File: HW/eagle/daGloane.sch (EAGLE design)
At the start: 44 parts, among them IC1 STM32F103CBT6, IC3 FT232RL, IC5 UA78M05DCY

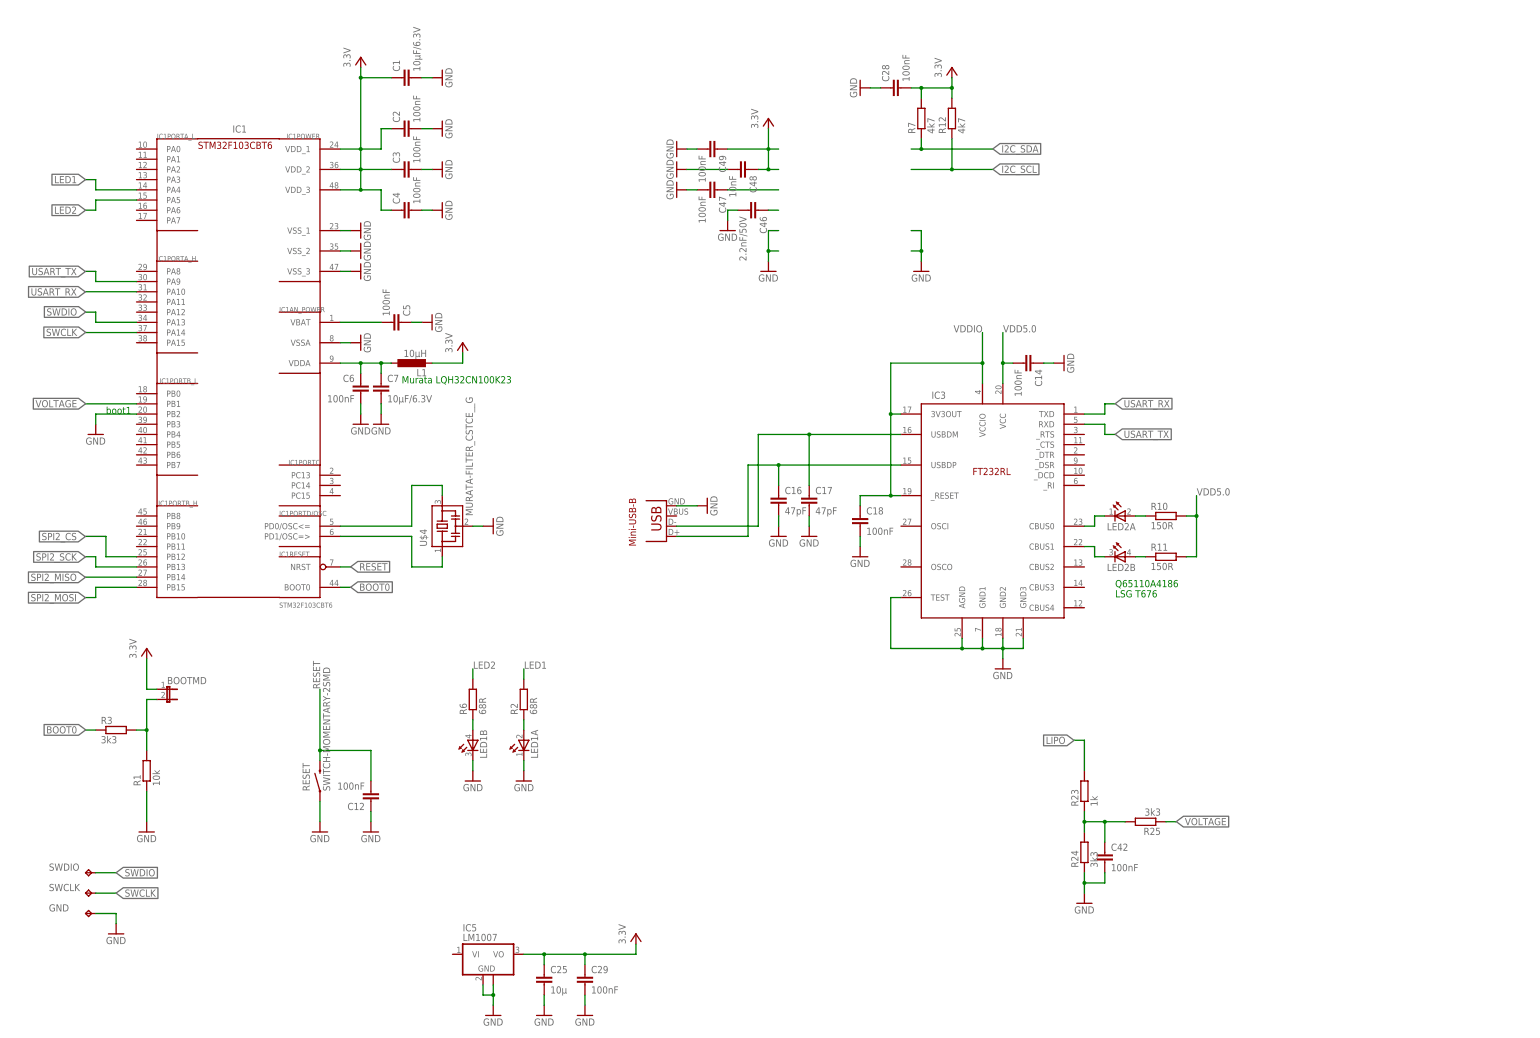
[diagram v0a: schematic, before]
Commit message: USB2UART interface replaced MPU6000 added
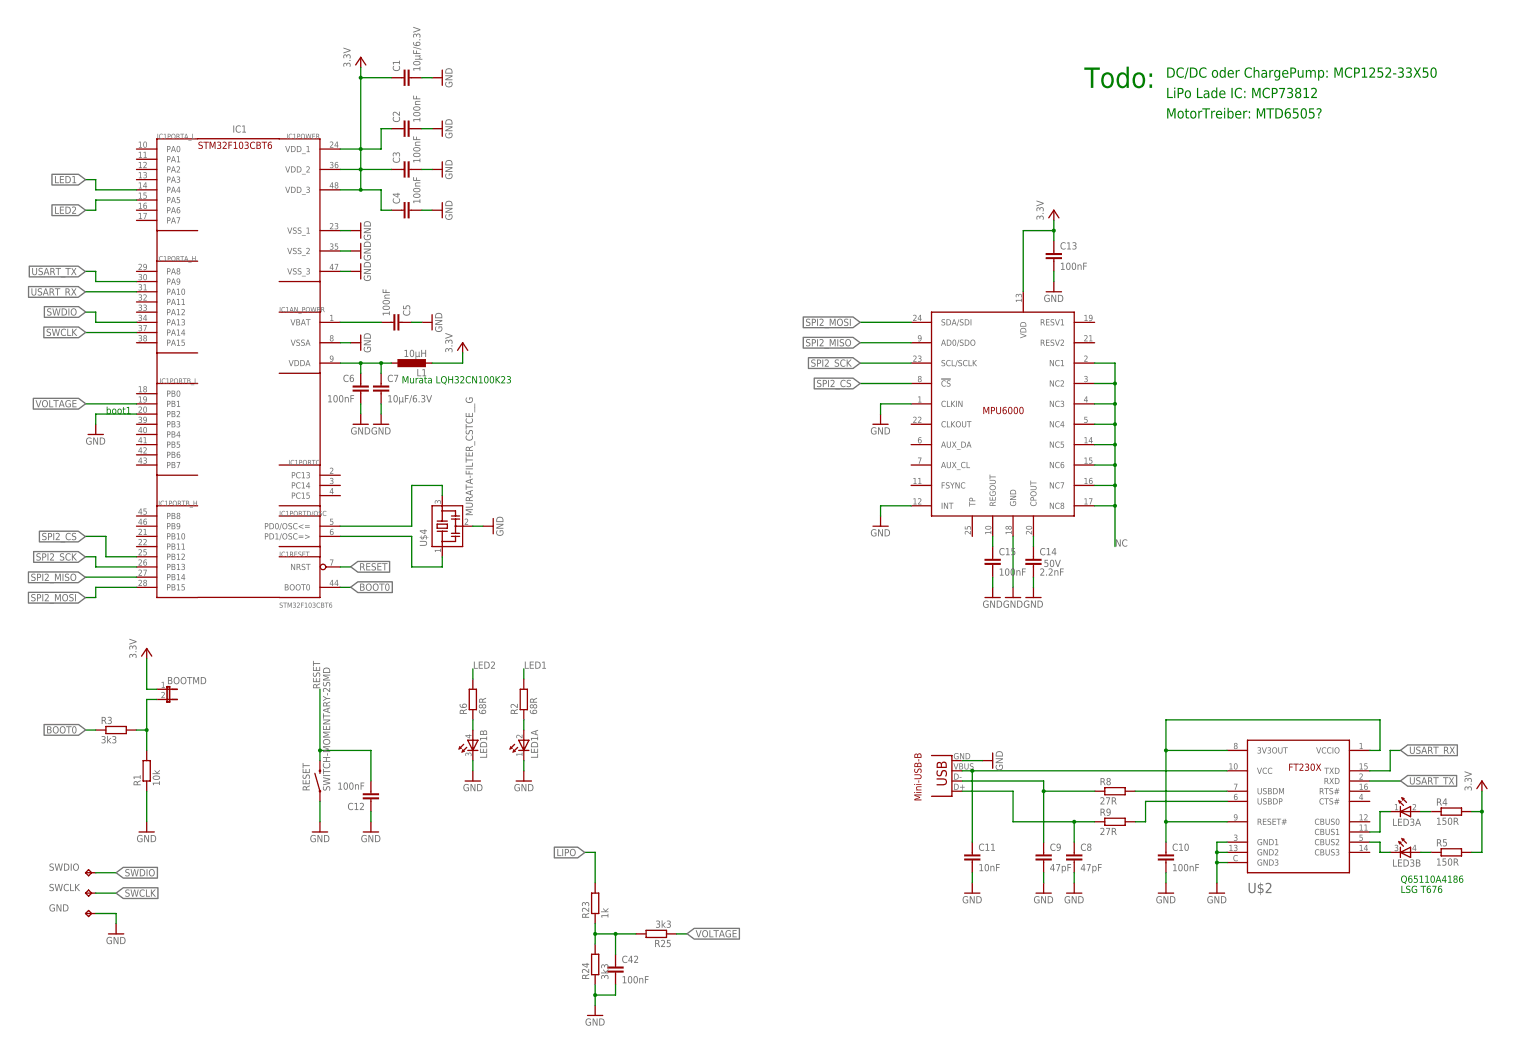
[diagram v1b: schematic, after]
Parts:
- removed C16, C17: 47pF, rcl:C-EUC0805
- removed C18, C28, C29, C47, C49: 100nF, rcl:C-EUC0805
- removed C25: 10µ, rcl:C-EUC0805
- removed C46: 2.2nF/50V, rcl:C-EUC0805
- removed C48: 10nF, rcl:C-EUC0805
- removed IC3: FT232RL, ftdichip:FT232RL
- removed IC5: UA78M05DCY, linear:UA78M05DCY
- removed LED2: (no value), led:TOPLED-2-MPI
- removed R10, R11: 150R, rcl:R-EU_R0805
- removed R12, R7: 4k7, rcl:R-EU_R0805
- added C10, C13, C15: 100nF, rcl:C-EUC0805
- added C11: 10nF, rcl:C-EUC0805
- added C8, C9: 47pF, rcl:C-EUC0805
- added LED3: (no value), led:TOPLED-2-MPI
- added R4, R5: 150R, rcl:R-EU_R0805
- added R8, R9: 27R, rcl:R-EU_R0805
- added U$1: MPU6000, MPU6000:MPU6000
- added U$2: SERIAL_FT230XQ, ftdiftx:SERIAL_FT230XQ
- C14: value 100nF -> 2.2nF; VOLTAGE (none) -> 50V
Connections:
- removed net I2C_SCL: R12.1
- removed net I2C_SDA: R7.1
- removed net N$13: C47.1
- removed net N$4: LED2A.A, R10.1
- removed net VDD5.0: C14.2, IC3.VCC, R10.2, R11.2
- removed net VDDIO: C18.1, IC3.3V3OUT, IC3.VCCIO, IC3._RESET
- new net N$11: LED3A.C, U$2.CBUS1
- new net N$12: LED3B.C, U$2.CBUS2
- new net N$14: LED3A.A, R4.1
- new net N$15: LED3B.A, R5.1
- new net N$16: R8.2, U$2.USBDM
- new net N$17: R9.2, U$2.USBDP
- new net NC: U$1.NC1, U$1.NC2, U$1.NC3, U$1.NC4, U$1.NC5, U$1.NC6, U$1.NC7, U$1.NC8
- net D+: now also C8.1, R9.1; no longer C16.1, IC3.USBDP
- net D-: now also C9.1, R8.1; no longer C17.1, IC3.USBDM
- net GND: now also C10.2, C11.2, C13.2, C14.2, C15.2, C8.2, C9.2, U$1.CLKIN, U$1.GND, U$1.INT, U$2.GND1, U$2.GND2, U$2.GND3; no longer C14.1, C16.2, C17.2, C18.2, C25.2, C28.1, C29.2, C46.2, C47.2, C48.2, C49.2, IC3.AGND, IC3.GND1, IC3.GND2, IC3.GND3, IC3.TEST, IC5.GND, IC5.GND@1
- net N$2: now also C10.1, U$2.3V3OUT, U$2.RESET#, U$2.VCCIO; no longer IC3.CBUS0, LED2A.C
- net N$3: now also C11.1, U$2.VCC, USB2.VBUS; no longer IC3.CBUS1, LED2B.C
- net N$5: now also C14.1, U$1.CPOUT; no longer LED2B.A, R11.1
- net N$6: now also C15.1, U$1.REGOUT; no longer C46.1
- net SPI2_CS: now also U$1.!CS
- net SPI2_MISO: now also U$1.AD0/SDO
- net SPI2_MOSI: now also U$1.SDA/SDI
- net SPI2_SCK: now also U$1.SCL/SCLK
- net USART_RX: now also U$2.TXD; no longer IC3.TXD
- net USART_TX: now also U$2.RXD; no longer IC3.RXD
- net VCC: now also C13.1, R4.2, R5.2, U$1.VDD; no longer C25.1, C28.2, C29.1, C48.1, C49.1, IC5.VO, R12.2, R7.2
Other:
- note added: "DC/DC oder ChargePump: MCP1252-33X50"
- note added: "FT230X"
- note added: "LiPo Lade IC: MCP73812"
- note added: "MotorTreiber: MTD6505?"
- note added: "Todo:"
- note removed: "FT232RL"
- moved on the sheet: C14, C42, R23, R24, R25

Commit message: package size of passive components reduced to 0603 dual LED replaced by standart LEDs in 0805 package
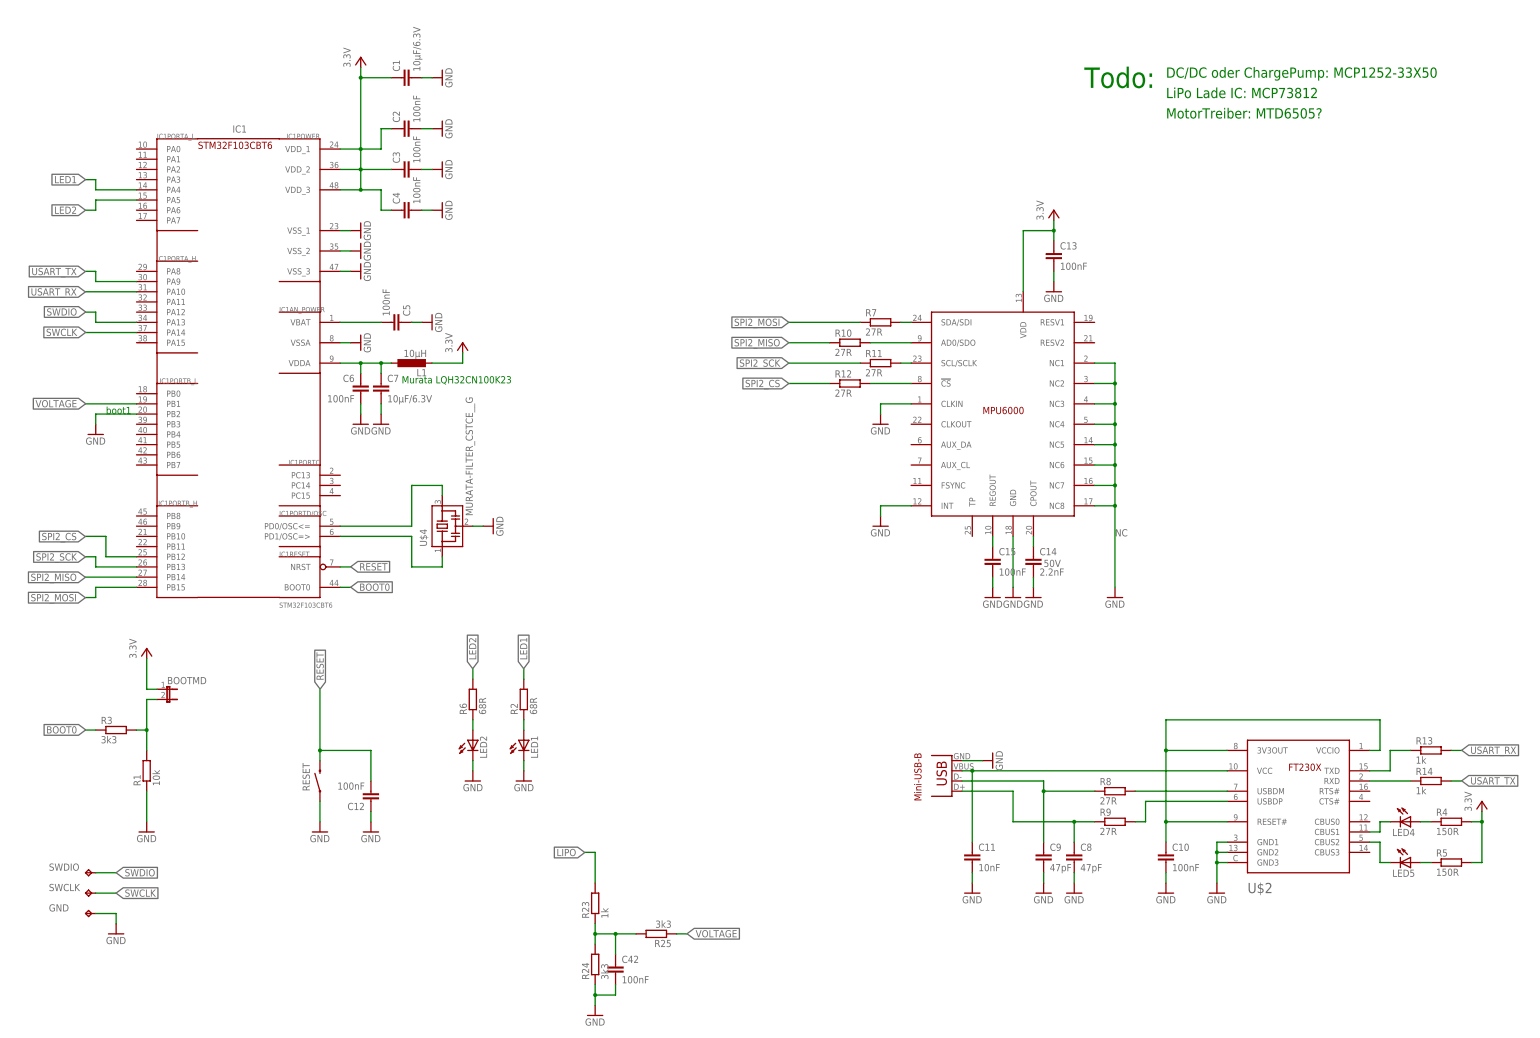
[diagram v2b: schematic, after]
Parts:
- removed LED3: (no value), led:TOPLED-2-MPI
- added LED2, LED4, LED5: (no value), led:LEDCHIPLED_0805
- added R10, R11, R12, R7: 27R, rcl:R-EU_R0603
- added R13, R14: 1k, rcl:R-EU_R0603
- C10, C11, C12, C13, C14, C15, C2, C3, C4, C42, C5, C6, C8, C9: device rcl:C-EUC0805 -> rcl:C-EUC0603
- LED1: device led:TOPLED-2-MPI -> led:LEDCHIPLED_0805
- R1, R2, R23, R24, R25, R3, R4, R5, R6, R8, R9: device rcl:R-EU_R0805 -> rcl:R-EU_R0603
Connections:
- new net N$13: R11.2, U$1.SCL/SCLK
- new net N$18: R10.2, U$1.AD0/SDO
- new net N$19: R7.2, U$1.SDA/SDI
- new net N$20: R13.1, U$2.TXD
- new net N$21: R14.1, U$2.RXD
- new net N$4: R12.2, U$1.!CS
- net GND: now also LED1.C, LED2.C; no longer LED1A.C, LED1B.C
- net N$11: now also LED4.C; no longer LED3A.C
- net N$12: now also LED5.C; no longer LED3B.C
- net N$14: now also LED4.A; no longer LED3A.A
- net N$15: now also LED5.A; no longer LED3B.A
- net N$8: now also LED1.A; no longer LED1A.A
- net N$9: now also LED2.A; no longer LED1B.A
- net SPI2_CS: now also R12.1; no longer U$1.!CS
- net SPI2_MISO: now also R10.1; no longer U$1.AD0/SDO
- net SPI2_MOSI: now also R7.1; no longer U$1.SDA/SDI
- net SPI2_SCK: now also R11.1; no longer U$1.SCL/SCLK
- net USART_RX: now also R13.2; no longer U$2.TXD
- net USART_TX: now also R14.2; no longer U$2.RXD
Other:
- note removed: "LSG T676"
- note removed: "Q65110A4186"
- moved on the sheet: R4, R5

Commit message: -MCP1252 added: Low Noise,  Positive-Regulated Charge Pump (Lipo 3..4.2V -> 3.3V) -MCP73831 added: Single Cell, Fully Integrated Li-Ion,Li-Polymer Charge Management Controller (USB Batterie Charging)
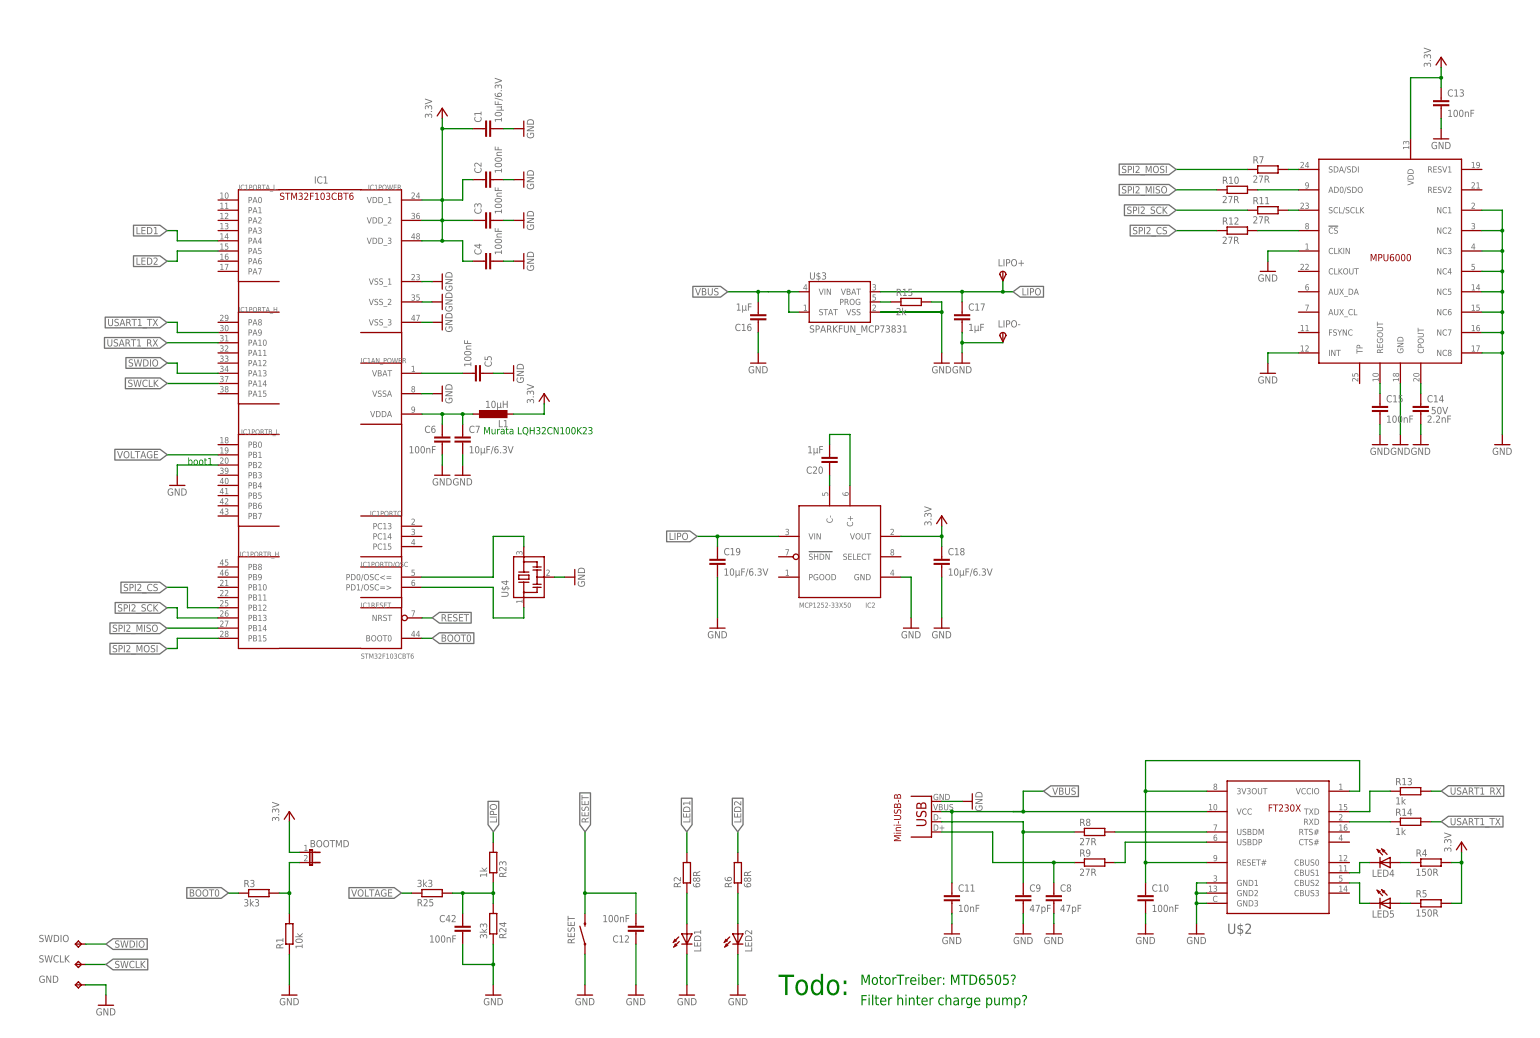
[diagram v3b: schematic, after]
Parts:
- added C16, C17, C20: 1µF, rcl:C-EUC0805
- added C18, C19: 10µF/6.3V, rcl:C-EUC0805
- added IC2: MCP1252-33X50, microchip-MCP125x-xxx:MCP1252-33X50
- added LIPO+, LIPO-: TPSPAD1-13Y, testpad:TPSPAD1-13Y
- added R15: 2k, rcl:R-EU_R0603
- added U$3: SPARKFUN_MCP73831, LiPo-USB-Charger-v21:SPARKFUN_MCP73831
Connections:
- net USART_RX renamed USART1_RX
- net USART_TX renamed USART1_TX
- removed net NC: U$1.NC1, U$1.NC2, U$1.NC3, U$1.NC4, U$1.NC5, U$1.NC6, U$1.NC7, U$1.NC8
- new net N$24: C20.2, IC2.C+
- new net N$28: C20.1, IC2.C-
- new net VBUS: C11.1, C16.2, U$2.VCC, U$3.STAT, U$3.VIN, USB2.VBUS
- net GND: now also C16.1, C17.2, C18.2, C19.2, IC2.GND, LIPO-.PP, R15.2, U$1.NC1, U$1.NC2, U$1.NC3, U$1.NC4, U$1.NC5, U$1.NC6, U$1.NC7, U$1.NC8, U$3.VSS
- net LIPO: now also C17.1, C19.1, IC2.VIN, LIPO+.PP, U$3.VBAT
- net N$1: now also IC1PORTD/OSC.PD1/OSC=>
- net N$3: now also R15.1, U$3.PROG; no longer C11.1, U$2.VCC, USB2.VBUS
- net N$7: now also IC1PORTD/OSC.PD0/OSC<=
- net VCC: now also C18.1, IC2.VOUT
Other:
- note added: "Filter hinter charge pump?"
- note removed: "DC/DC oder ChargePump: MCP1252-33X50"
- note removed: "LiPo Lade IC: MCP73812"
- moved on the sheet: BOOTMD, C1, C10, C11, C12, C13, C14, C15, C2, C3, C4, C42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

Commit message: tacticle switch and nesessacy circuitry  for power on/off added.    leakage current might become an issure..
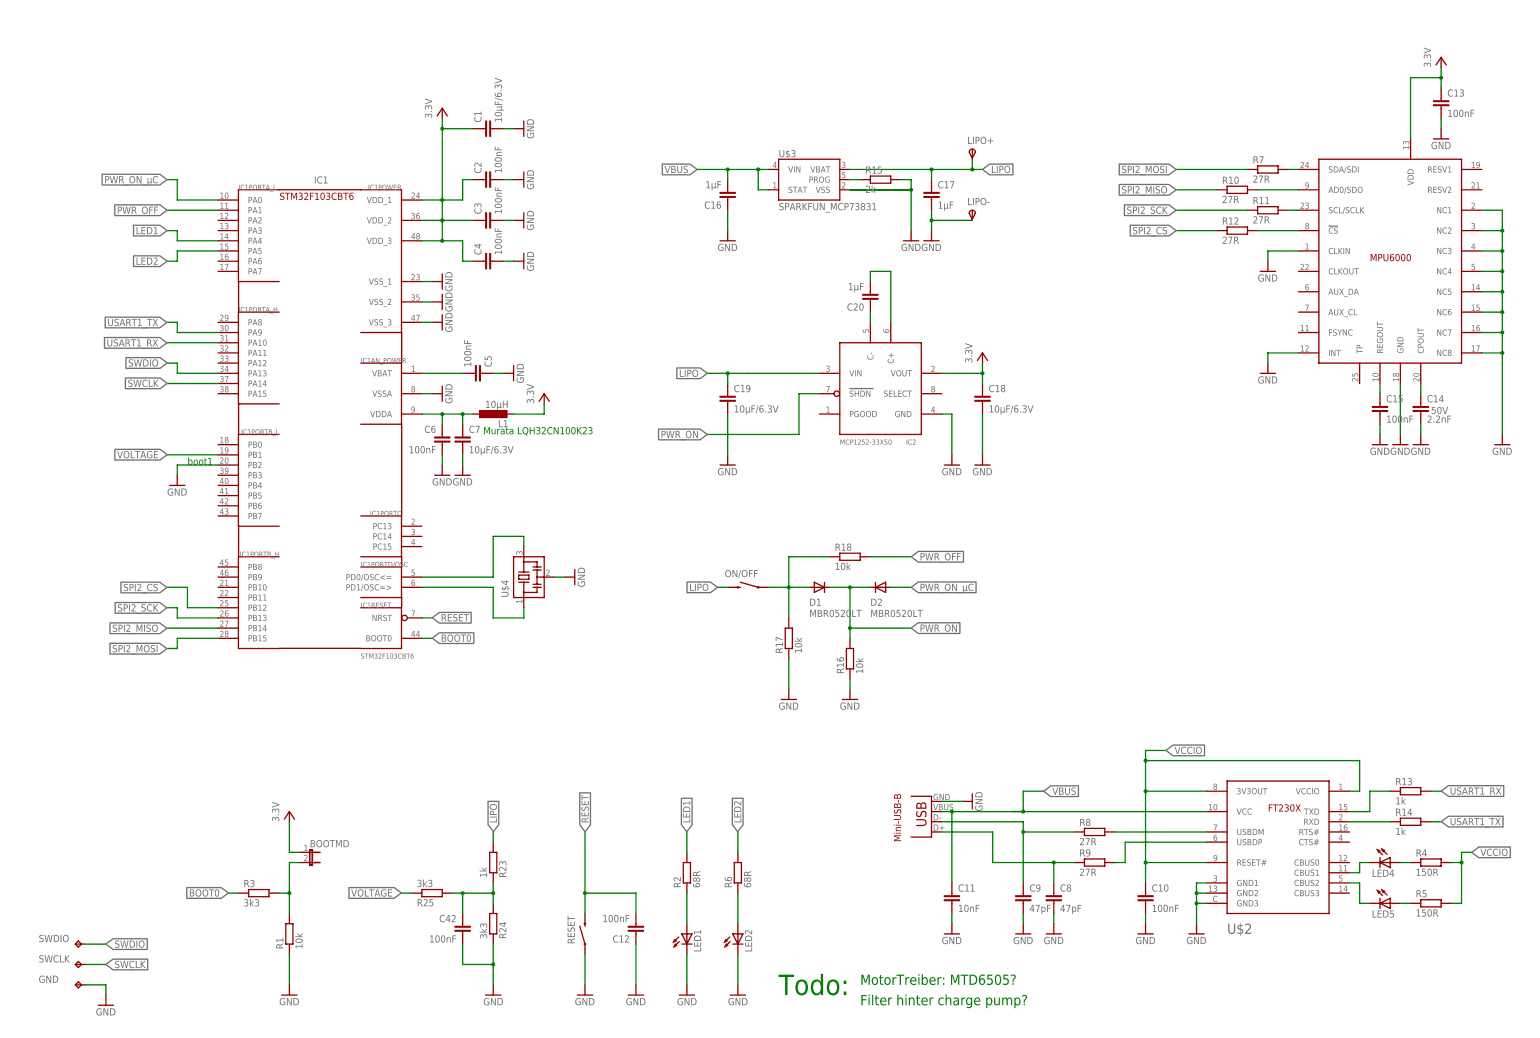
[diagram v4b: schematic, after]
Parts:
- added D1, D2: MBR0520LT, diode:MBR0520LT
- added ON/OFF: SWITCH-MOMENTARY-2SMD, SparkFun-Electromechanical:SWITCH-MOMENTARY-2SMD
- added R16, R17, R18: 10k, rcl:R-EU_R0603
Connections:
- removed net N$2: C10.1, U$2.3V3OUT, U$2.RESET#, U$2.VCCIO
- new net N$23: D1.A, ON/OFF.1, R17.2, R18.1
- new net PWR_OFF: IC1PORTA_L.PA1, R18.2
- new net PWR_ON: D1.C, D2.C, IC2.SHDN, R16.2
- new net PWR_ON_µC: D2.A, IC1PORTA_L.PA0
- new net VCCIO: C10.1, R4.2, R5.2, U$2.3V3OUT, U$2.RESET#, U$2.VCCIO
- net GND: now also R16.1, R17.1
- net LIPO: now also ON/OFF.2
- net VCC: no longer R4.2, R5.2
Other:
- moved on the sheet: C16, C17, C18, C19, C20, IC2, LIPO+, LIPO-, R15, U$3
